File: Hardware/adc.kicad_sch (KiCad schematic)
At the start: 14 parts, among them U2 NAU7802SGI, Y1 Crystal_GND23

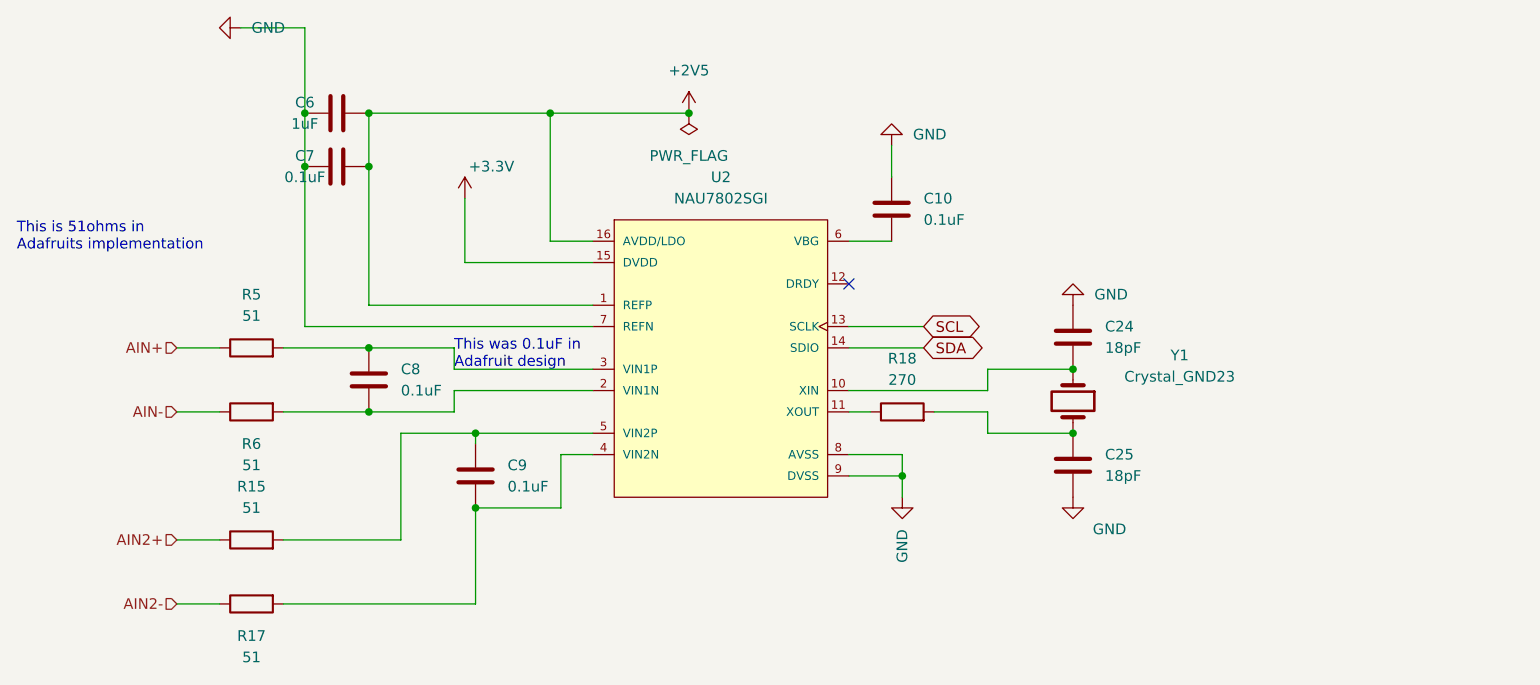
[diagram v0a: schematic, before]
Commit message: in the absence of design docs, I just did my own thing.  I've kept the ribbon cable, but I am not sure why there are one on either side, I've also brought out most of the interrupt lines on the through hole headers, the headers are designed for placement on a carrier board, negating the need for the ribbon cable when the board is stacked
Signed-off-by: lokimetasmith <lokimail@gmail.com>
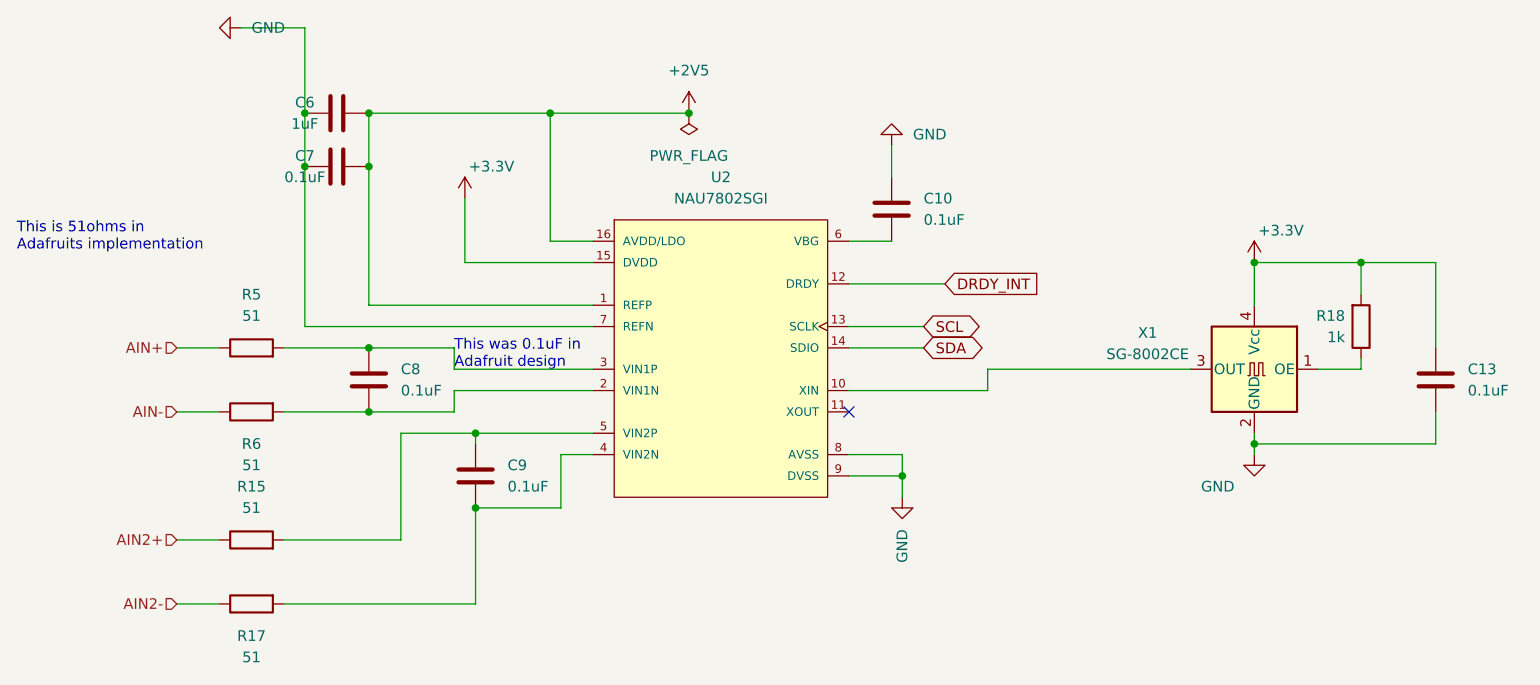
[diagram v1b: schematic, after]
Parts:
- removed C24, C25: 18pF, Capacitor_SMD:C_0603_1608Metric_Pad1.08x0.95mm_HandSolder, symbol Device:C
- removed Y1: Crystal_GND23, Crystal:Crystal_SMD_HC49-SD, symbol Device:Crystal
- added C13: 0.1uF, Capacitor_SMD:C_0603_1608Metric_Pad1.08x0.95mm_HandSolder, symbol Device:C
- added X1: SG-8002CE, Oscillator:Oscillator_SMD_SeikoEpson_SG8002CE-4Pin_3.2x2.5mm, symbol Oscillator:SG-8002CE
- R18: value 270 -> 1k
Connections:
- net +3V3: now also R18.2, C13.1, X1.4 (Vcc)
- net GND: now also C13.2, X1.2 (GND)
- net at U2.10 (XIN): now also X1.3 (OUT)
- net at U2.11 (XOUT): no longer R18.1
- net DRDY_INT: now reaches U2.12 (DRDY)
- new net: R18.1, X1.1 (OE)
